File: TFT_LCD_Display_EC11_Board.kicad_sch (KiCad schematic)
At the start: 29 parts, among them J2 Control, J3 I2C, J4 TFT-LCD-DISPLAY-EC11, J5 USB_C_Receptacle_USB2.0_16P, Q1 BC848, Q2 BC848, U1 LM2937-3.3V, U2 USBLC6-2SC6, U3 ESP32-WROVER-E-N4R8, U4 CP2104

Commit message: Tweede Commit
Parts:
- renumbered J5 to J1, R7 to R1, R8 to R2, TP4 to TP3, TP5 to TP4, TP6 to TP5
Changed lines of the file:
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@@
 		(dnp no)
 		(fields_autoplaced yes)
-		(property "Reference" "#PWR06"
+		(property "Reference" "#PWR05"
 			(at 105.41 69.85 0)
 			(hide yes)
@@
 			(project "TFT_LCD_Display_EC11_Board"
 				(path "/3c59e70f-e9c5-4ef4-a932-269e9554ea5b"
-					(reference "#PWR06")
+					(reference "#PWR05")
 					(unit 1)
 				)
@@
 		(dnp no)
 		(fields_autoplaced yes)
-		(property "Reference" "#PWR014"
+		(property "Reference" "#PWR02"
 			(at 44.45 115.57 0)
 			(hide yes)
@@
 			(project "TFT_LCD_Display_EC11_Board"
 				(path "/3c59e70f-e9c5-4ef4-a932-269e9554ea5b"
-					(reference "#PWR014")
+					(reference "#PWR02")
 					(unit 1)
 				)
@@
 		(in_pos_files yes)
 		(dnp no)
-		(property "Reference" "R8"
+		(property "Reference" "R2"
 			(at 64.516 78.74 90)
 			(show_name no)
@@
 			(project "TFT_LCD_Display_EC11_Board"
 				(path "/3c59e70f-e9c5-4ef4-a932-269e9554ea5b"
-					(reference "R8")
+					(reference "R2")
 					(unit 1)
 				)
@@
 		(dnp no)
 		(fields_autoplaced yes)
-		(property "Reference" "#PWR09"
+		(property "Reference" "#PWR07"
 			(at 151.13 184.15 0)
 			(hide yes)
@@
 			(project "TFT_LCD_Display_EC11_Board"
 				(path "/3c59e70f-e9c5-4ef4-a932-269e9554ea5b"
-					(reference "#PWR09")
+					(reference "#PWR07")
 					(unit 1)
 				)
@@
 		(dnp no)
 		(fields_autoplaced yes)
-		(property "Reference" "TP4"
+		(property "Reference" "TP3"
 			(at 73.787 19.6158 0)
 			(show_name no)
@@
 			(project "TFT_LCD_Display_EC11_Board"
 				(path "/3c59e70f-e9c5-4ef4-a932-269e9554ea5b"
-					(reference "TP4")
+					(reference "TP3")
 					(unit 1)
 				)
@@
 		(dnp no)
 		(fields_autoplaced yes)
-		(property "Reference" "#PWR013"
+		(property "Reference" "#PWR04"
 			(at 72.39 83.82 0)
 			(hide yes)
@@
 			(project "TFT_LCD_Display_EC11_Board"
 				(path "/3c59e70f-e9c5-4ef4-a932-269e9554ea5b"
-					(reference "#PWR013")
+					(reference "#PWR04")
 					(unit 1)
 				)
@@
 		(in_pos_files yes)
 		(dnp no)
-		(property "Reference" "R7"
+		(property "Reference" "R1"
 			(at 64.516 76.2 90)
 			(show_name no)
@@
 			(project "TFT_LCD_Display_EC11_Board"
 				(path "/3c59e70f-e9c5-4ef4-a932-269e9554ea5b"
-					(reference "R7")
+					(reference "R1")
 					(unit 1)
 				)
@@
 		(dnp no)
 		(fields_autoplaced yes)
-		(property "Reference" "#PWR011"
+		(property "Reference" "#PWR09"
 			(at 251.46 120.65 0)
 			(hide yes)
@@
 			(project "TFT_LCD_Display_EC11_Board"
 				(path "/3c59e70f-e9c5-4ef4-a932-269e9554ea5b"
-					(reference "#PWR011")
+					(reference "#PWR09")
 					(unit 1)
 				)
@@
 		(dnp no)
 		(fields_autoplaced yes)
-		(property "Reference" "#PWR07"
+		(property "Reference" "#PWR06"
 			(at 137.16 97.79 0)
 			(hide yes)
@@
 			(project "TFT_LCD_Display_EC11_Board"
 				(path "/3c59e70f-e9c5-4ef4-a932-269e9554ea5b"
-					(reference "#PWR07")
+					(reference "#PWR06")
 					(unit 1)
 				)
@@
 		(in_pos_files yes)
 		(dnp no)
-		(property "Reference" "TP5"
+		(property "Reference" "TP4"
 			(at 189.23 38.608 0)
 			(show_name no)
@@
 			(project "TFT_LCD_Display_EC11_Board"
 				(path "/3c59e70f-e9c5-4ef4-a932-269e9554ea5b"
-					(reference "TP5")
+					(reference "TP4")
 					(unit 1)
 				)
@@
 		(dnp no)
 		(fields_autoplaced yes)
-		(property "Reference" "J5"
+		(property "Reference" "J1"
 			(at 44.45 64.4355 0)
 			(show_name no)
@@
 			(project "TFT_LCD_Display_EC11_Board"
 				(path "/3c59e70f-e9c5-4ef4-a932-269e9554ea5b"
-					(reference "J5")
+					(reference "J1")
 					(unit 1)
 				)
@@
 		(dnp no)
 		(fields_autoplaced yes)
-		(property "Reference" "#PWR015"
+		(property "Reference" "#PWR01"
 			(at 36.83 115.57 0)
 			(hide yes)
@@
 			(project "TFT_LCD_Display_EC11_Board"
 				(path "/3c59e70f-e9c5-4ef4-a932-269e9554ea5b"
-					(reference "#PWR015")
+					(reference "#PWR01")
 					(unit 1)
 				)
@@
 		(in_pos_files yes)
 		(dnp no)
-		(property "Reference" "TP6"
+		(property "Reference" "TP5"
 			(at 189.992 68.072 0)
 			(show_name no)
@@
 			(project "TFT_LCD_Display_EC11_Board"
 				(path "/3c59e70f-e9c5-4ef4-a932-269e9554ea5b"
-					(reference "TP6")
+					(reference "TP5")
 					(unit 1)
 				)
@@
 		(dnp no)
 		(fields_autoplaced yes)
-		(property "Reference" "#PWR010"
+		(property "Reference" "#PWR08"
 			(at 241.3 101.6 0)
 			(hide yes)
@@
 			(project "TFT_LCD_Display_EC11_Board"
 				(path "/3c59e70f-e9c5-4ef4-a932-269e9554ea5b"
-					(reference "#PWR010")
+					(reference "#PWR08")
 					(unit 1)
 				)

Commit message: 3D Files
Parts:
- added Cx4: 100nF, Capacitor_SMD:C_1206_3216Metric_Pad1.33x1.80mm_HandSolder, symbol Device:C
- added Rx7, Rx8: 10k, Resistor_SMD:R_1206_3216Metric_Pad1.30x1.75mm_HandSolder, symbol Device:R
- C3: footprint Capacitor_SMD:C_0805_2012Metric_Pad1.18x1.45mm_HandSolder -> Capacitor_SMD:C_1206_3216Metric_Pad1.33x1.80mm_HandSolder
- R1, R2: footprint Resistor_SMD:R_0805_2012Metric_Pad1.20x1.40mm_HandSolder -> Resistor_SMD:R_1206_3216Metric_Pad1.30x1.75mm_HandSolder
- TP1, TP2, TP3, TP4, TP5: footprint TestPoint:TestPoint_Loop_D3.80mm_Drill2.0mm -> TestPoint:TestPoint_Loop_D2.50mm_Drill1.0mm
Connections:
- net 3v3: now also Rx7.2, Rx8.1
- net GND: now also Cx4.2
- net GPIO0: now also Rx8.2
- net RESET: now also Rx7.1
- net ~{ENABLE}: now also Cx4.1
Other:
- moved on the sheet: JP1, R6

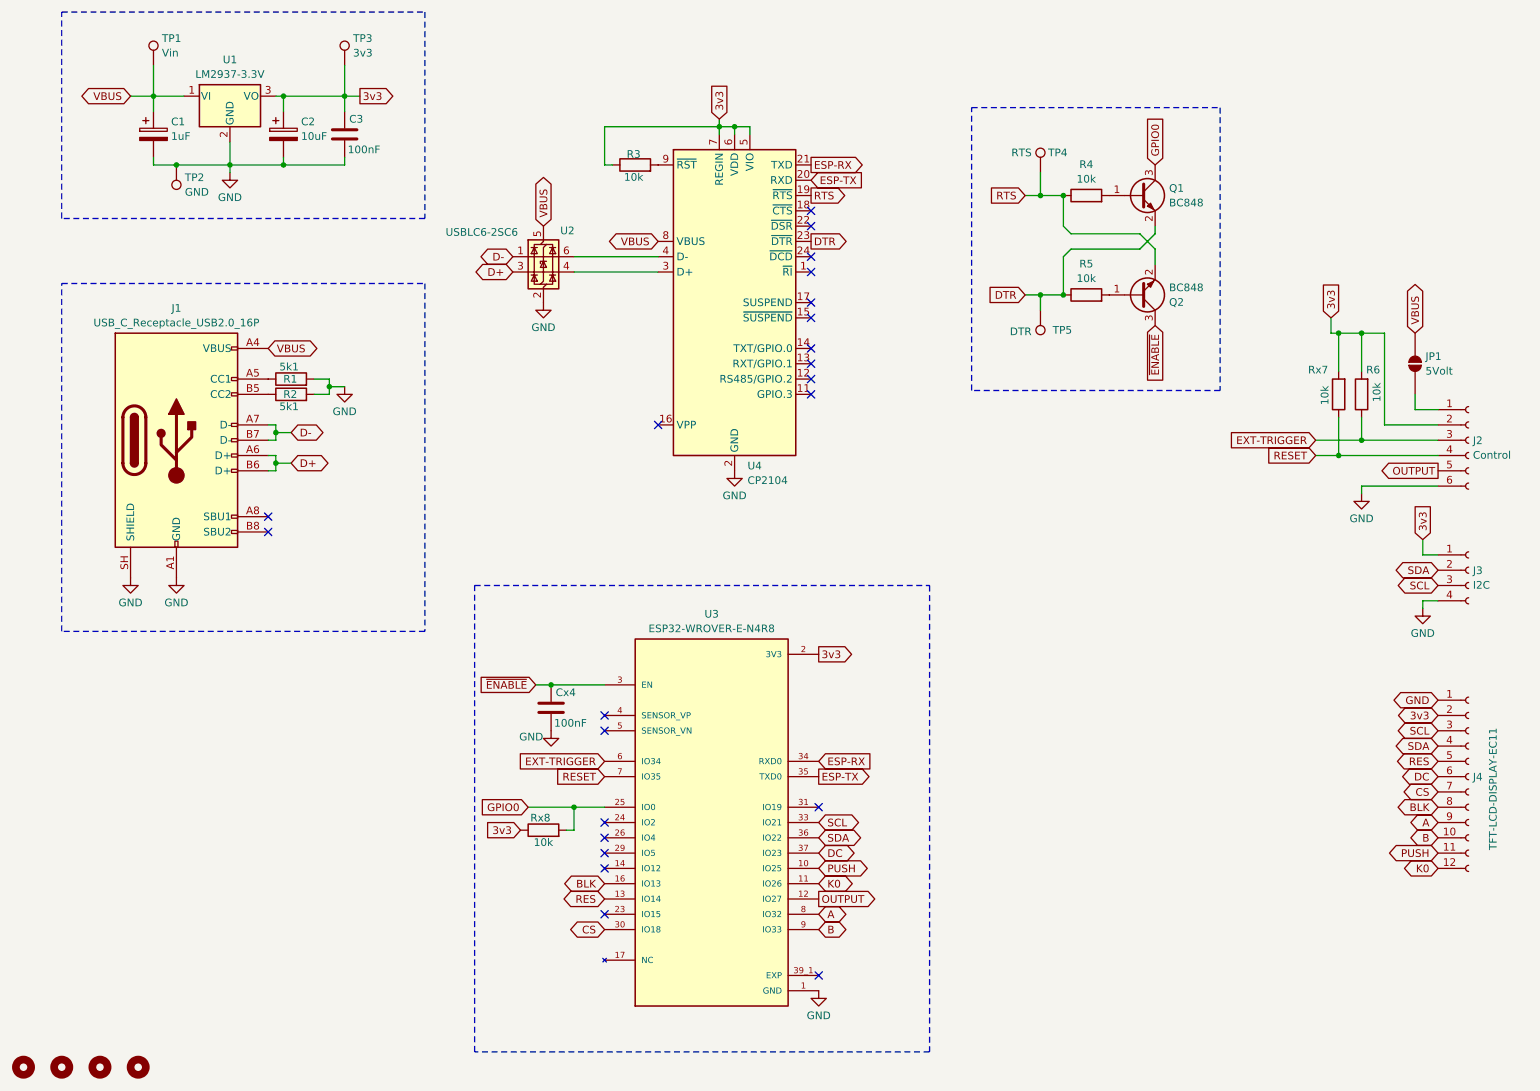
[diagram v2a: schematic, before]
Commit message: Combine Rev 2.0 and openSCAD files
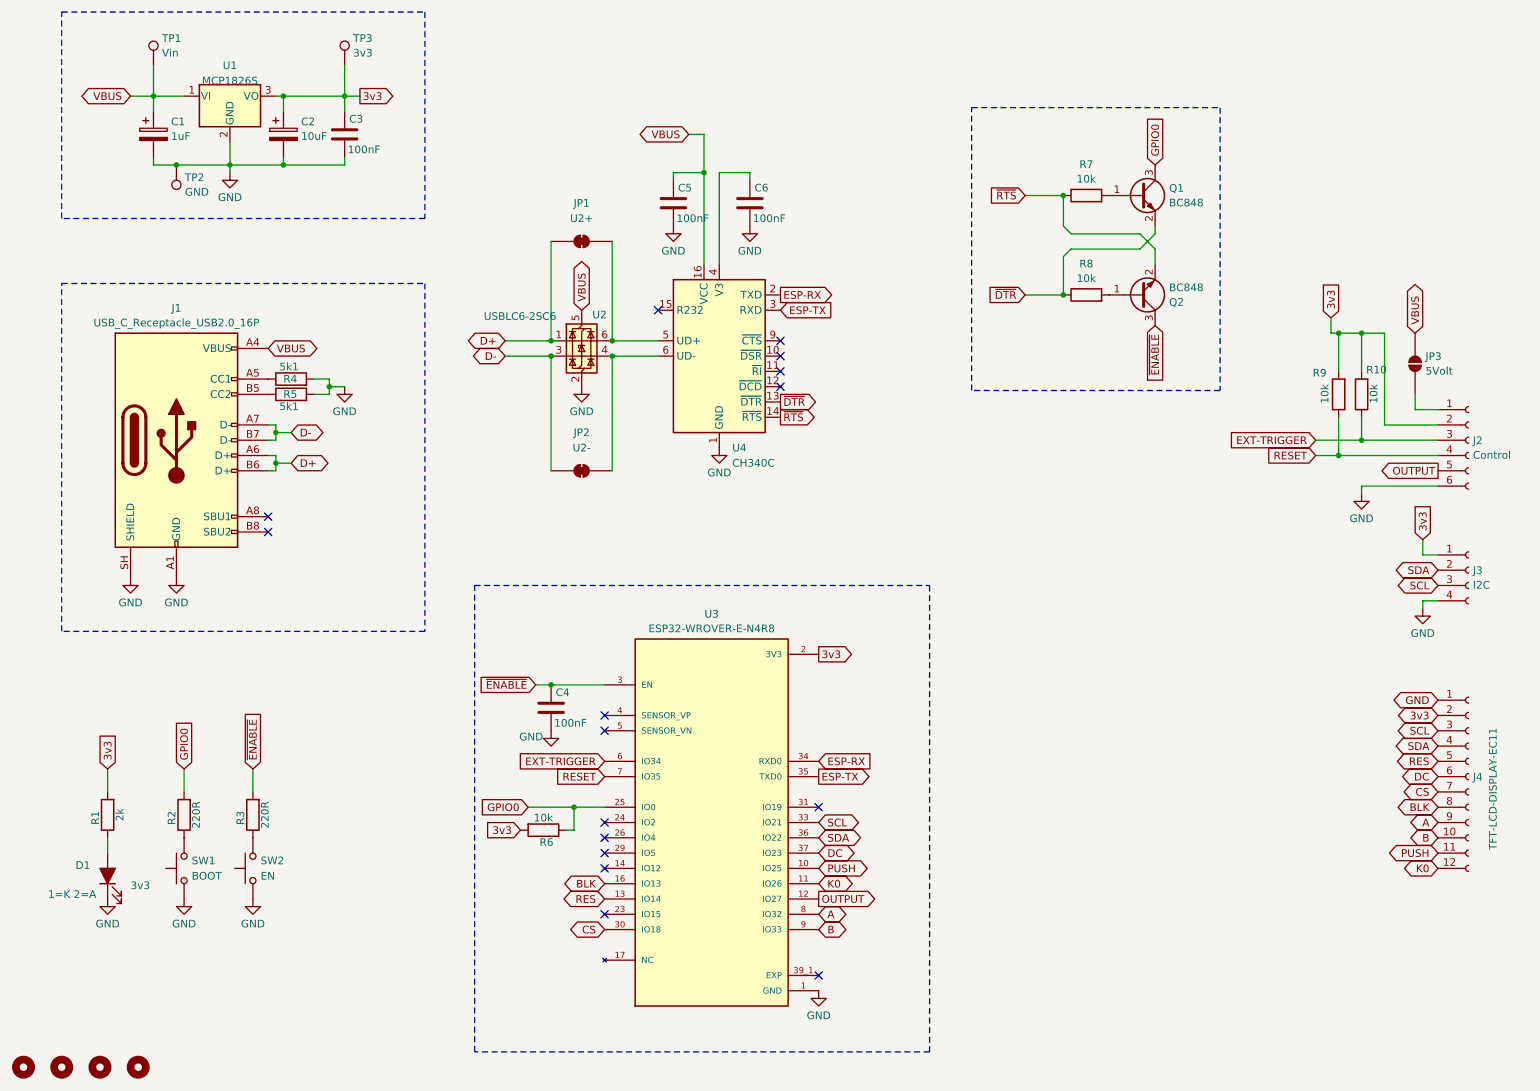
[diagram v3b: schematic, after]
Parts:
- removed Cx4: 100nF, Capacitor_SMD:C_1206_3216Metric_Pad1.33x1.80mm_HandSolder, symbol Device:C
- removed Rx7, Rx8: 10k, Resistor_SMD:R_1206_3216Metric_Pad1.30x1.75mm_HandSolder, symbol Device:R
- removed TP4: RTS, TestPoint:TestPoint_Loop_D2.50mm_Drill1.0mm, symbol Connector:TestPoint
- removed TP5: DTR, TestPoint:TestPoint_Loop_D2.50mm_Drill1.0mm, symbol Connector:TestPoint
- removed U1: LM2937-3.3V, Package_TO_SOT_SMD:SOT-223, symbol Regulator_Linear:TC1262-33
- removed U4: CP2104, Package_DFN_QFN:QFN-24-1EP_4x4mm_P0.5mm_EP2.6x2.6mm, symbol Interface_USB:CP2104
- added C4, C5, C6: 100nF, Capacitor_SMD:C_1206_3216Metric_Pad1.33x1.80mm_HandSolder, symbol Device:C
- added D1: 3v3, LED_SMD:LED_1206_3216Metric_Pad1.42x1.75mm_HandSolder, symbol Device:LED_Filled
- added JP1: U2+, Jumper:SolderJumper-2_P1.3mm_Open_RoundedPad1.0x1.5mm, symbol Jumper:SolderJumper_2_Bridged
- added JP2: U2-, Jumper:SolderJumper-2_P1.3mm_Open_RoundedPad1.0x1.5mm, symbol Jumper:SolderJumper_2_Bridged
- added R1: 2k, Resistor_SMD:R_1206_3216Metric_Pad1.30x1.75mm_HandSolder, symbol Device:R
- added R2: 220R, Resistor_SMD:R_1206_3216Metric_Pad1.30x1.75mm_HandSolder, symbol Device:R
- added R6, R9: 10k, Resistor_SMD:R_1206_3216Metric_Pad1.30x1.75mm_HandSolder, symbol Device:R
- added SW1: BOOT, Button_Switch_SMD:SW_SPST_FSMSM, symbol Switch:SW_Push
- added SW2: EN, Button_Switch_SMD:SW_SPST_FSMSM, symbol Switch:SW_Push
- added U1: MCP1826S, Package_TO_SOT_SMD:SOT-223-3_TabPin2, symbol Regulator_Linear:MCP1826S
- added U4: CH340C, Package_SO:SOIC-16_3.9x9.9mm_P1.27mm, symbol Interface_USB:CH340C
- R3: value 10k -> 220R
- U3: footprint myNewLibrary:XCVR_ESP32-WROVER-E-N4R8 -> MyNewLibrary:ESP32-WROVER-B-E
- renumbered JP1 to JP3, R6 to R10, R1 to R4, R2 to R5, R4 to R7, R5 to R8
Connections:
- net 3v3: now also R1.2, R6.2, R9.2, U1.3 (VO); no longer R3.1
- net D+: now also U2.1 (I/O1), JP1.1 (A); no longer U2.3 (I/O2)
- net D-: now also U2.3 (I/O2), JP2.1 (A); no longer U2.1 (I/O1)
- net ESP-RX: now also U4.2 (TXD)
- net ESP-TX: now also U4.3 (RXD)
- net GND: now also C4.2, C5.2, C6.2, D1.1 (K), SW1.1, SW2.1, U1.2 (GND), U4.1 (GND)
- net GPIO0: now also R2.2, R6.1
- net RESET: now also R9.1
- net VBUS: now also C5.1, U1.1 (VI), U4.16 (VCC)
- net ~{ENABLE}: now also R3.2, C4.1
- net at U2.4 (I/O2): now also JP2.2 (B), U4.6 (UD-)
- net at U2.6 (I/O1): now also JP1.2 (B), U4.5 (UD+)
- net DTR renamed ~{DTR}
- net ~{DTR}: now also U4.13 (~{DTR})
- net RTS renamed ~{RTS}
- net ~{RTS}: now also U4.14 (~{RTS})
- new net: R3.1, SW2.2
- new net: R2.1, SW1.2
- new net: D1.2 (A), R1.1
- new net: C6.1, U4.4 (V3)
- no-connect marks 22 -> 16
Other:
- moved on the sheet: U2
